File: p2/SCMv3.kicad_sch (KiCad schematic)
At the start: 120 parts, among them IC1 40106, IC2 40106, IC3 TL082, J1 ISP, J1-OUT8 JACK-MONO-SWB, J2 Conn_01x02, J2-OUT7 JACK-MONO-SWB, J3 POWER, J3-OUT6 JACK-MONO-SWB, J4-OUT5 JACK-MONO-SWB, J5-OUT4 JACK-MONO-SWB, J6-OUT3 JACK-MONO-SWB, J7-OUT2 JACK-MONO-SWB, J8-OUT1 JACK-MONO-SWB, J9-CLK_IN1 JCLK_IN, Q1 Si2318, Q2 Si2318, Q3 Si2318, Q4 Si2318, U1 ATMEGA328-AU, Y1 16MHz_18pF_FA238

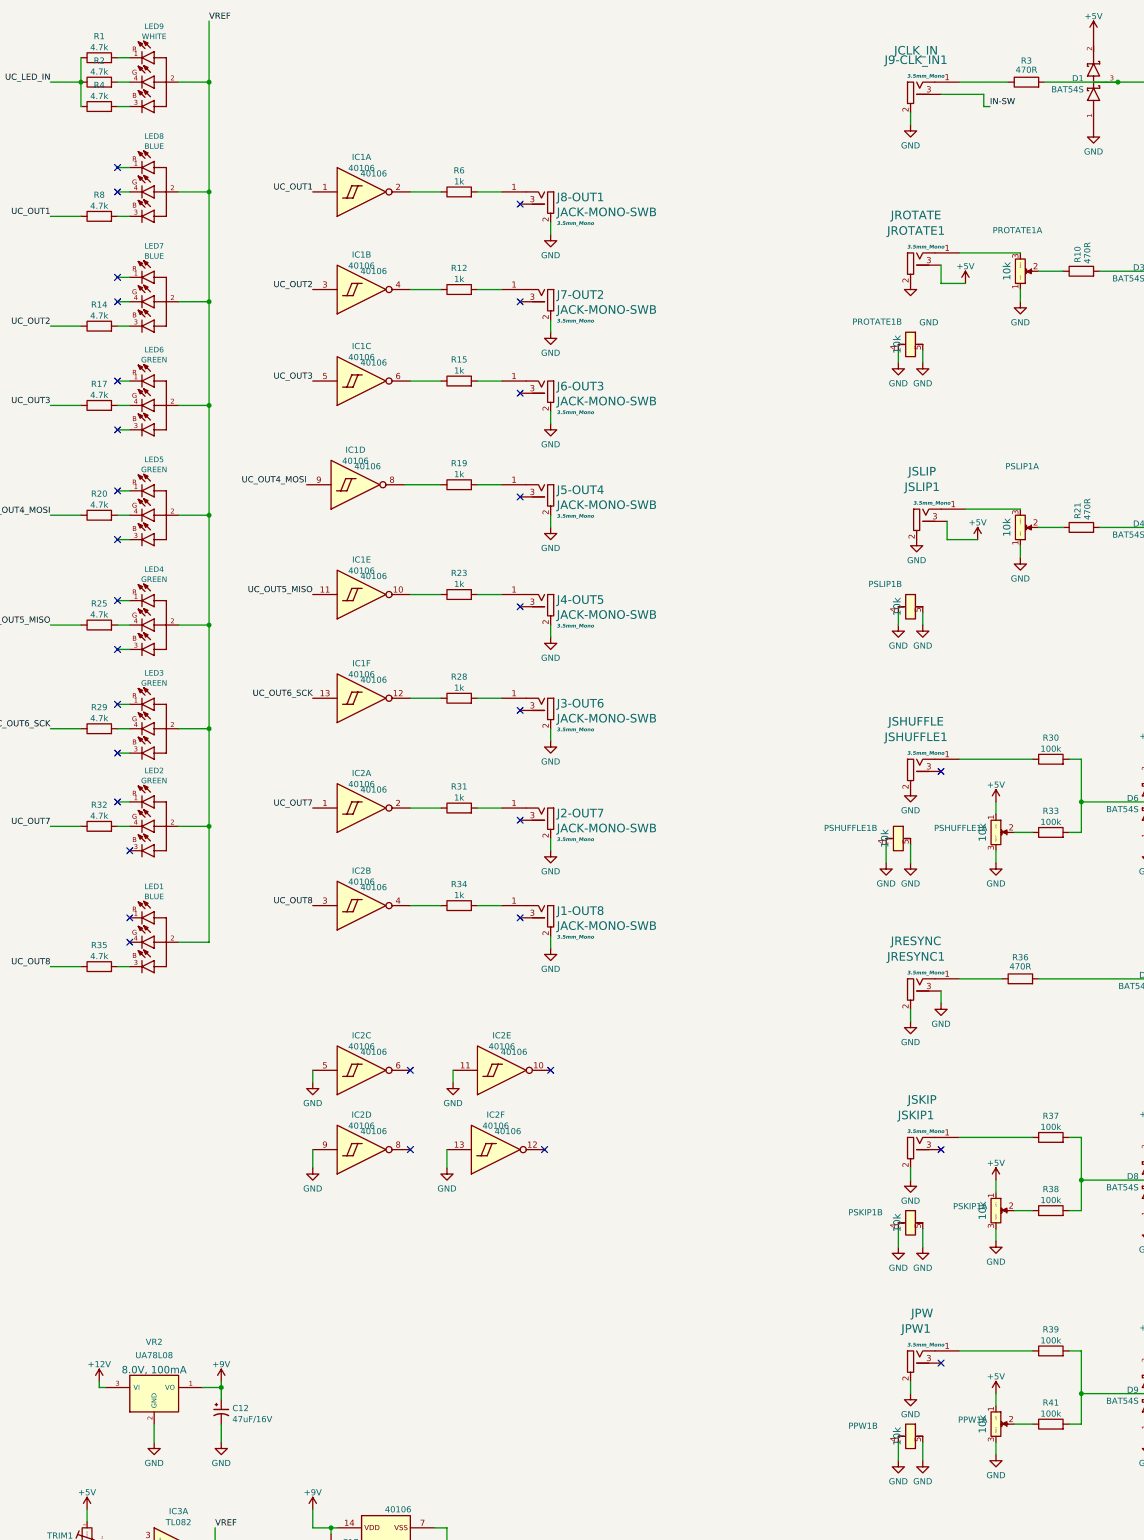
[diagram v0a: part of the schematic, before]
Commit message: SCMBOV3 updates
Updated resistor value to fix blueness of white led 
Changed the pot footprints on schematic and pcb 
Flipped shuffle/skip/pw pots so they are not longer backward on sch and pcb
sorry if I staged too many things I was not sure...
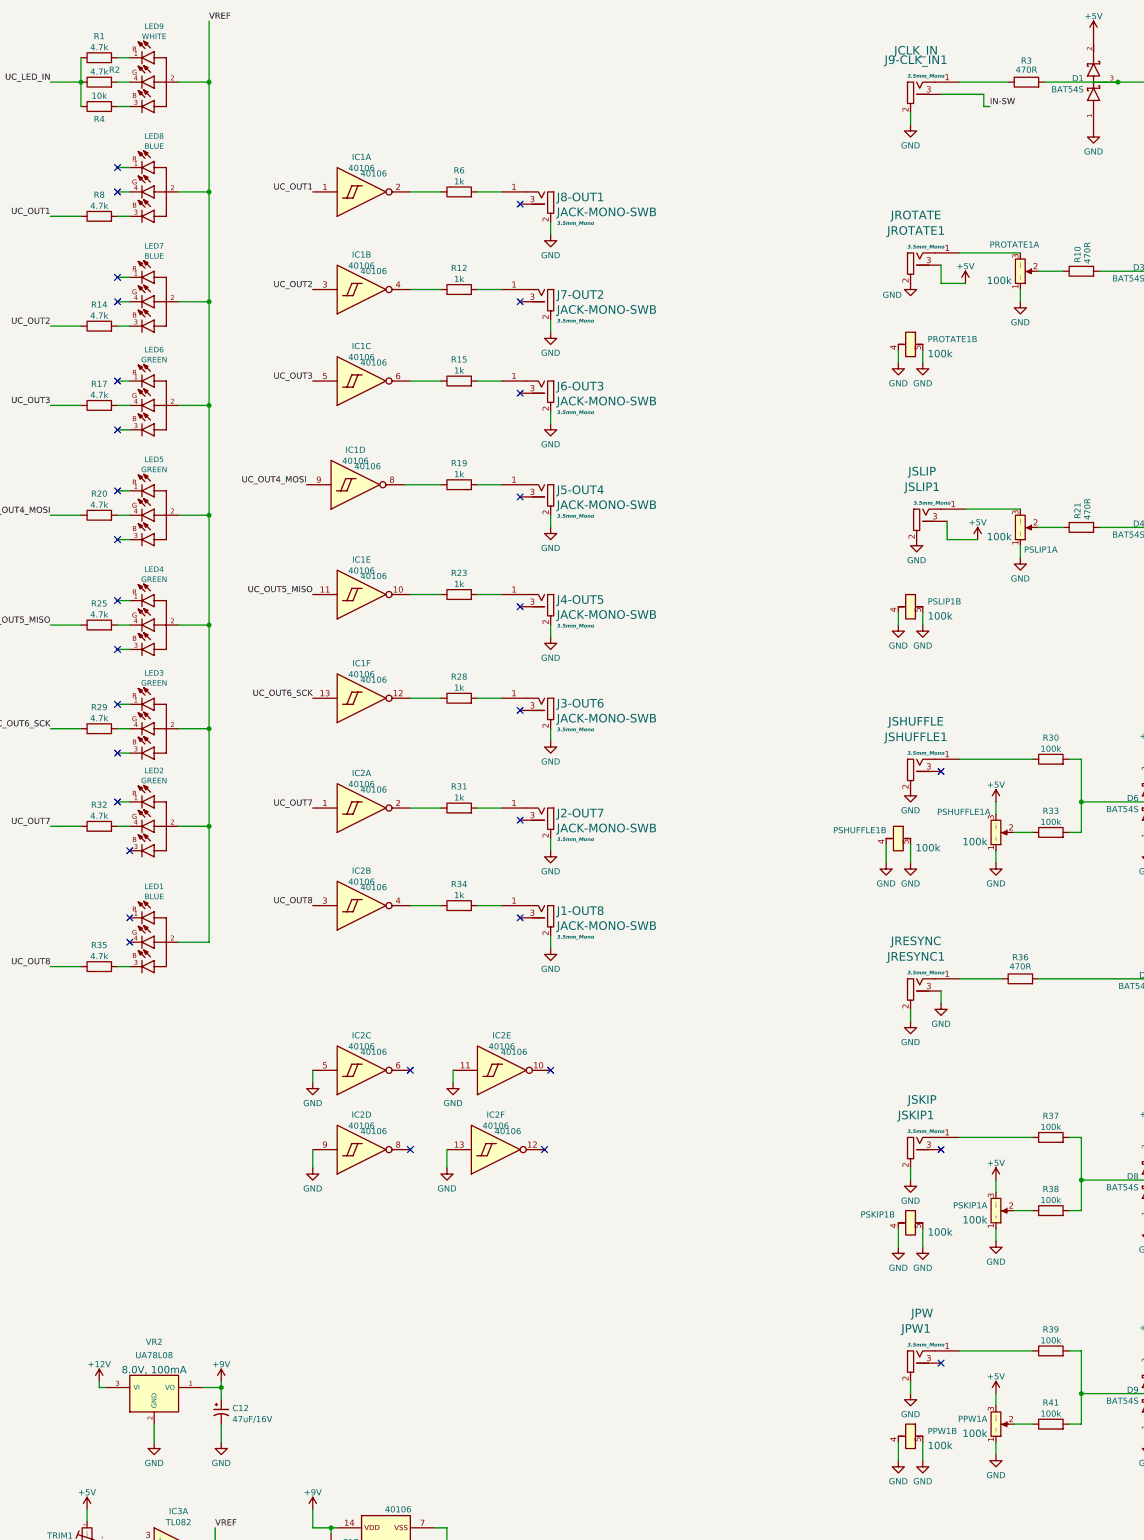
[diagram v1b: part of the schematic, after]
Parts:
- removed PPW1, PROTATE1, PSHUFFLE1, PSKIP1, PSLIP1: 9mm_CtrDet_10k_DShaft, 4ms_Potentiometer:Pot_9mm_Dshaft_Det, symbol 4ms_Potentiometer:9mm_CtrDet_10k_DShaft
- removed R4: 4.7k_0603, 4ms_Resistor:R_0603, symbol 4ms_Resistor:4.7k_0603
- added PPW1, PROTATE1, PSHUFFLE1, PSKIP1, PSLIP1: 9mm_NoDet_100k_Knurled_Lined, 4ms_Potentiometer:Pot_9mm_Knurl_NoDet, symbol 4ms_Potentiometer:9mm_NoDet_100k_Knurled_Lined
- added R4: 10k_0603, 4ms_Resistor:R_0603, symbol 4ms_Resistor:10k_0603
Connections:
- net +5V: now also PPW1.3 (Right), PSHUFFLE1.3 (Right), PSKIP1.3 (Right)
- net GND: now also PPW1.1 (Left), PPW1.4 (Tab1), PPW1.5 (Tab2), PROTATE1.1 (Left), PROTATE1.4 (Tab1), PROTATE1.5 (Tab2), PSHUFFLE1.1 (Left), PSHUFFLE1.4 (Tab1), PSHUFFLE1.5 (Tab2), PSKIP1.1 (Left), PSKIP1.4 (Tab1), PSKIP1.5 (Tab2), PSLIP1.1 (Left), PSLIP1.4 (Tab1), PSLIP1.5 (Tab2)
- net UC_LED_IN: now also R4.1
- net at R33.1: now also PSHUFFLE1.2 (Center)
- net at LED9.3 (CB): now also R4.2
- net at R38.1: now also PSKIP1.2 (Center)
- net at R41.1: now also PPW1.2 (Center)
- net at R21.1: now also PSLIP1.2 (Center)
- net at JSLIP1.1 (SIG): now also PSLIP1.3 (Right)
- net at JROTATE1.1 (SIG): now also PROTATE1.3 (Right)
- net at R10.1: now also PROTATE1.2 (Center)
